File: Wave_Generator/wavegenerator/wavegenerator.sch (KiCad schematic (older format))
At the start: 61 parts, among them J1 01x05, J2 USB_B_Micro, J3 Conn_Coaxial, J4 1x2Pinheader, SW1 button, SW2 button, SW3 SP3T, U1 AZ1117E-3.3, U2 ATmega328P-AU, U3 MC33063AD, U4 MAX038CPP, Y1 16MHz

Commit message: naming changes
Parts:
- J1: footprint wavegenerator_v1:01x05_pin_header -> wavegenerator:01x05_pin_header; symbol wavegenerator_v1:PinHeaders -> wavegenerator:PinHeaders
- J2: footprint wavegenerator_v1:USB_Micro-B_Amphenol_10118194-0001LF_Horizontal -> wavegenerator:USB_Micro-B_Amphenol_10118194-0001LF_Horizontal
- J3: footprint wavegenerator_v1:BNC_connector_731000105 -> wavegenerator:BNC_connector_731000105
- J4: symbol wavegenerator_v1:1x2Pinheader -> wavegenerator:1x2Pinheader
- MOD1: footprint wavegenerator_v1:TFT_LCD_ST7735 -> wavegenerator:TFT_LCD_ST7735; symbol wavegenerator_v1:TFT_LCD -> wavegenerator:TFT_LCD
- RV1, RV2, RV3: footprint wavegenerator_v1:Potentiometer_PTV09A -> wavegenerator:Potentiometer_PTV09A
- SW3: footprint wavegenerator_v1:SP3T_OS103011MS8QP1 -> wavegenerator:SP3T_OS103011MS8QP1; symbol wavegenerator_v1:SP3T_V1 -> wavegenerator:SP3T
- U4: footprint wavegenerator_v1:MAX038CPP-W -> wavegenerator:MAX038CPP-W; symbol wavegenerator_v1:MAX038CPP -> wavegenerator:MAX038CPP
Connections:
- wire segments 121 -> 118
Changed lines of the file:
@@
 EESchema Schematic File Version 4
-LIBS:wavegenerator_v1-cache
+LIBS:wavegenerator-cache
 EELAYER 29 0
 EELAYER END
@@
 F 0 "J2" H 5857 5417 50  0000 C CNN
 F 1 "USB_B_Micro" H 5857 5326 50  0000 C CNN
-F 2 "wavegenerator_v1:USB_Micro-B_Amphenol_10118194-0001LF_Horizontal" H 5950 4900 50  0001 C CNN
+F 2 "wavegenerator:USB_Micro-B_Amphenol_10118194-0001LF_Horizontal" H 5950 4900 50  0001 C CNN
 F 3 "~" H 5950 4900 50  0001 C CNN
 	1    5800 4950
@@
 $EndComp
 $Comp
-L wavegenerator_v1:MAX038CPP U4
+L wavegenerator:MAX038CPP U4
 U 1 1 5D1E353F
 P 3350 2400
 F 0 "U4" H 3350 3970 50  0000 C CNN
 F 1 "MAX038CPP" H 3350 3879 50  0000 C CNN
-F 2 "wavegenerator_v1:MAX038CPP-W" H 3350 2400 50  0001 L BNN
+F 2 "wavegenerator:MAX038CPP-W" H 3350 2400 50  0001 L BNN
 F 3 "" H 3350 2400 50  0001 L BNN
 F 4 "MAX038CPP" H 3350 2400 50  0001 L BNN "Field4"
@@
 F 0 "RV2" H 1481 1896 50  0000 R CNN
 F 1 "20k" H 1481 1805 50  0000 R CNN
-F 2 "wavegenerator_v1:Potentiometer_PTV09A" H 1550 1850 50  0001 C CNN
+F 2 "wavegenerator:Potentiometer_PTV09A" H 1550 1850 50  0001 C CNN
 F 3 "~" H 1550 1850 50  0001 C CNN
 	1    1550 1850
@@
 F 0 "RV1" V 2200 1300 50  0000 R CNN
 F 1 "1M" V 2100 1250 50  0000 R CNN
-F 2 "wavegenerator_v1:Potentiometer_PTV09A" H 2000 1300 50  0001 C CNN
+F 2 "wavegenerator:Potentiometer_PTV09A" H 2000 1300 50  0001 C CNN
 F 3 "~" H 2000 1300 50  0001 C CNN
 	1    2000 1300
@@
 	7800 1100 8000 1100
 $Comp
-L wavegenerator_v1:SP3T_V1 SW3
+L wavegenerator:SP3T SW3
 U 1 1 5D250C2F
 P 1500 2850
 F 0 "SW3" H 1250 2350 50  0000 C CNN
 F 1 "SP3T" H 1250 2450 50  0000 C CNN
-F 2 "wavegenerator_v1:SP3T_OS103011MS8QP1" H 1500 2800 50  0001 C CNN
+F 2 "wavegenerator:SP3T_OS103011MS8QP1" H 1500 2800 50  0001 C CNN
 F 3 "" H 1500 2800 50  0001 C CNN
 	1    1500 2850
@@
 $EndComp
 $Comp
-L wavegenerator_v1:TFT_LCD MOD1
+L wavegenerator:TFT_LCD MOD1
 U 1 1 5D34C1D1
 P 8600 4400
 F 0 "MOD1" H 9728 3396 50  0000 L CNN
 F 1 "TFT_LCD" H 9728 3305 50  0000 L CNN
-F 2 "wavegenerator_v1:TFT_LCD_ST7735" H 9050 4350 50  0001 C CNN
+F 2 "wavegenerator:TFT_LCD_ST7735" H 9050 4350 50  0001 C CNN
 F 3 "" H 9050 4350 50  0001 C CNN
 	1    8600 4400
@@
 $EndComp
 $Comp
-L wavegenerator_v1:PinHeaders J1
+L wavegenerator:PinHeaders J1
 U 1 1 5D2280FD
 P 10200 800
 F 0 "J1" H 10100 850 50  0000 C CNN
 F 1 "01x05" H 10100 750 50  0000 C CNN
-F 2 "wavegenerator_v1:01x05_pin_header" H 10200 800 50  0001 C CNN
+F 2 "wavegenerator:01x05_pin_header" H 10200 800 50  0001 C CNN
 F 3 "~" H 10200 800 50  0001 C CNN
 	1    10200 800
@@
 $EndComp
 $Comp
-L wavegenerator_v1:1x2Pinheader J4
+L wavegenerator:1x2Pinheader J4
 U 1 1 5D3E4848
 P 5850 2200
@@
 F 0 "J3" H 6300 2700 50  0000 L CNN
 F 1 "Conn_Coaxial" H 6200 2600 50  0000 L CNN
-F 2 "wavegenerator_v1:BNC_connector_731000105" H 6350 2450 50  0001 C CNN
+F 2 "wavegenerator:BNC_connector_731000105" H 6350 2450 50  0001 C CNN
 F 3 " ~" H 6350 2450 50  0001 C CNN
 	1    6350 2450
@@
 	1550 1300 1750 1300
 Wire Wire Line
-	4050 3200 4050 2950
-Connection ~ 4050 2950
-Wire Wire Line
 	4050 3500 4050 3650
-Connection ~ 4050 3650
 Wire Wire Line
 	4050 3400 4200 3400
@@
 F 0 "RV3" H 4200 2000 50  0000 C CNN
 F 1 "1k" H 4200 2100 50  0000 C CNN
-F 2 "wavegenerator_v1:Potentiometer_PTV09A" H 4350 2050 50  0001 C CNN
+F 2 "wavegenerator:Potentiometer_PTV09A" H 4350 2050 50  0001 C CNN
 F 3 "~" H 4350 2050 50  0001 C CNN
 	1    4350 2050
@@
 Connection ~ 4700 1850
 Wire Wire Line
-	4050 2950 4050 2700
-Connection ~ 4050 2700
-Wire Wire Line
-	4050 2700 4050 2450
-Connection ~ 4050 3200
-Wire Wire Line
-	2650 3050 2650 3250
-Connection ~ 2650 3450
-Connection ~ 2650 3250
-Wire Wire Line
-	2650 3250 2650 3450
-Wire Wire Line
 	4350 2250 4600 2250
 Wire Wire Line
@@
 Wire Wire Line
 	4600 2050 4700 2050
+Wire Wire Line
+	4050 2450 4050 3200
+Wire Wire Line
+	2650 3050 2650 3450
 $EndSCHEMATC

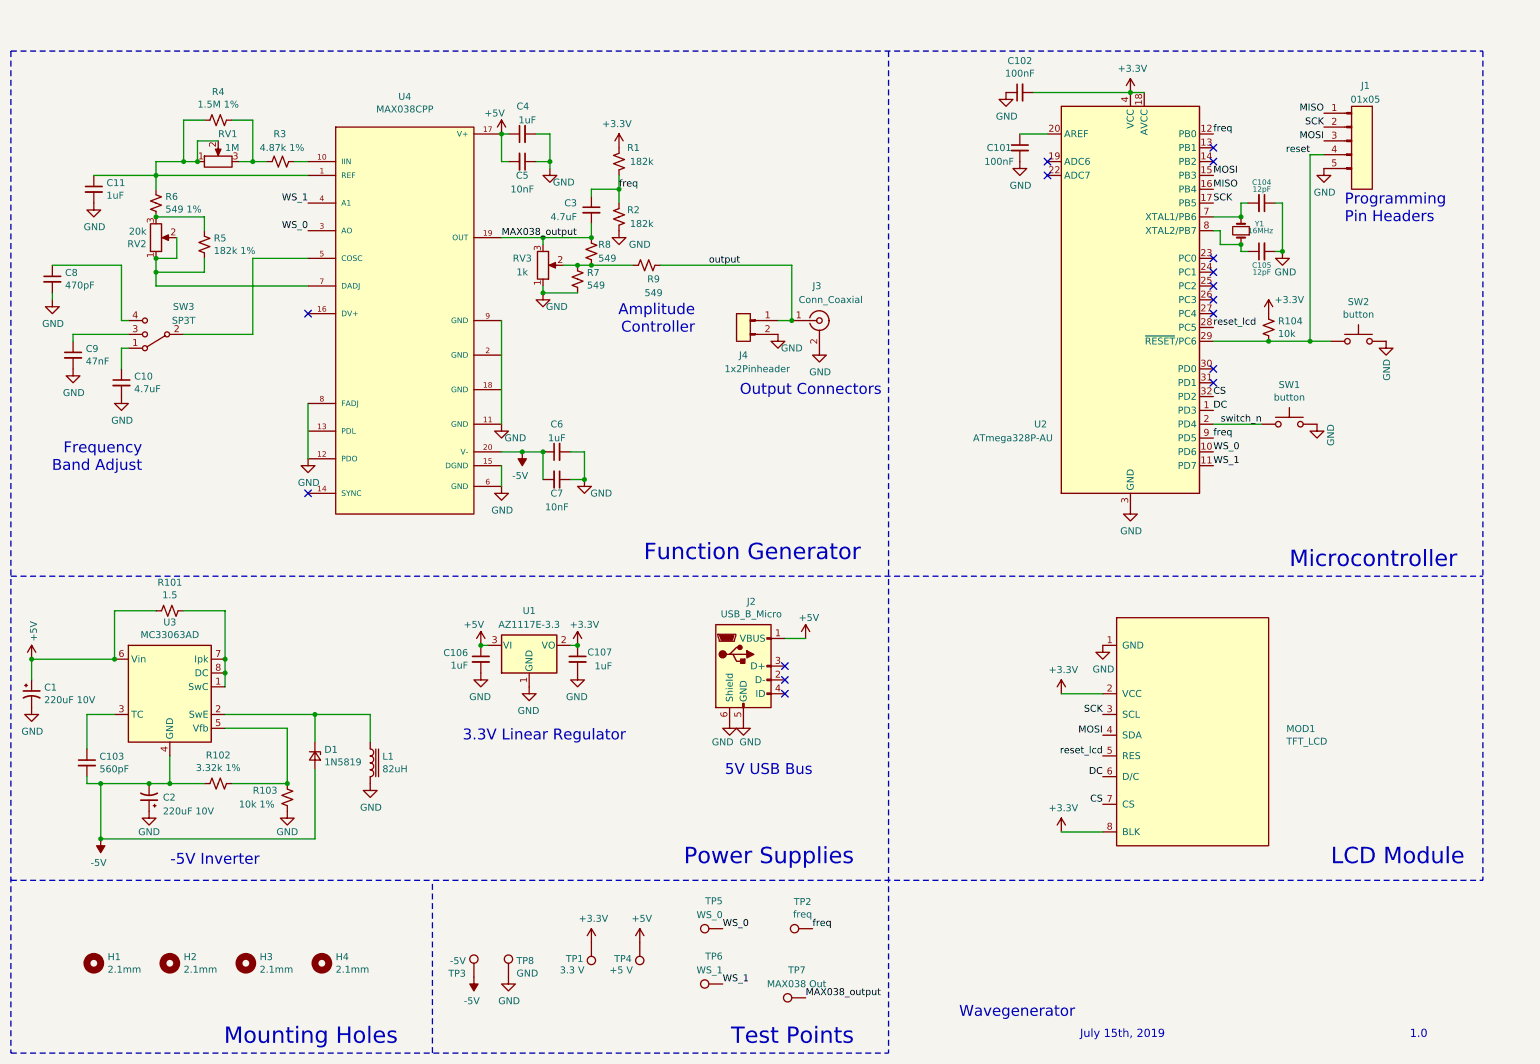
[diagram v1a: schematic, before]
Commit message: function generator schematic changes
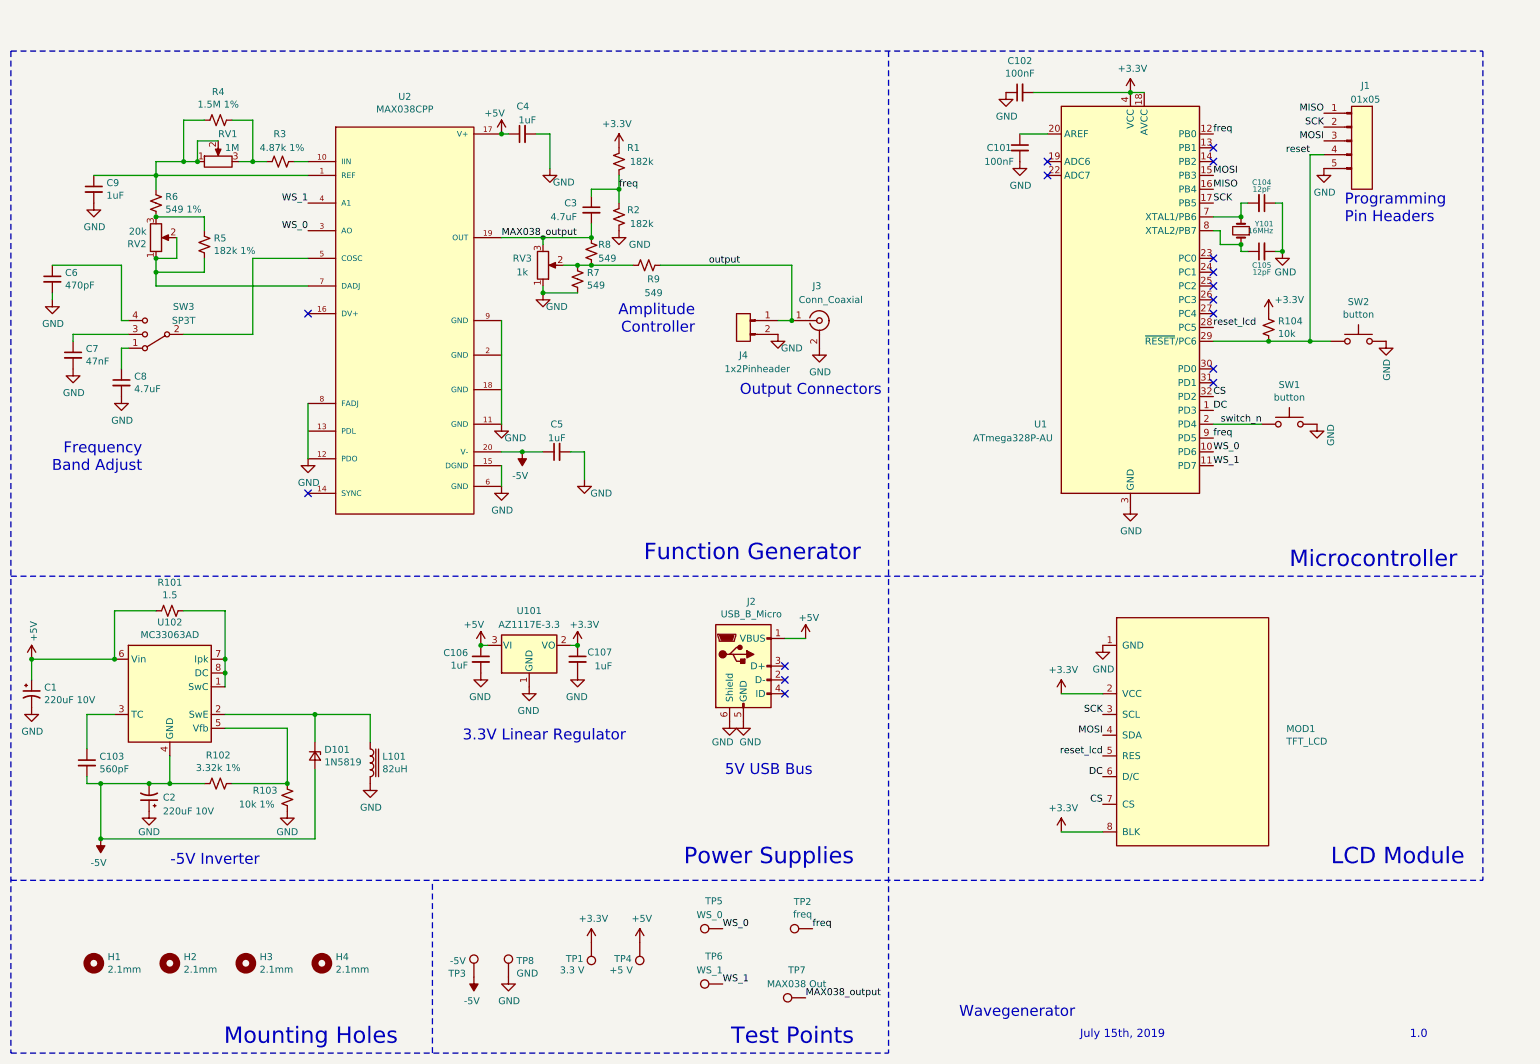
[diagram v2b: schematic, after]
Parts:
- removed C5, C7: 10nF, Capacitor_THT:C_Rect_L4.0mm_W2.5mm_P2.50mm, symbol Device:C_Small
- renumbered C6 to C5, C8 to C6, C9 to C7, C10 to C8, C11 to C9, D1 to D101, L1 to L101, U2 to U1, U1 to U101, U3 to U102, U4 to U2, Y1 to Y101
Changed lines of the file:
@@
 Connection ~ 1650 5800
 $Comp
-L Device:D_Zener_Small D1
+L Device:D_Zener_Small D101
 U 1 1 5D1C049C
 P 2700 5600
-F 0 "D1" V 2654 5668 50  0000 L CNN
+F 0 "D101" V 2654 5668 50  0000 L CNN
 F 1 "1N5819" V 2745 5668 50  0000 L CNN
 F 2 "Diode_SMD:D_SOD-123" V 2700 5600 50  0001 C CNN
@@
 $EndComp
 $Comp
-L Device:L_Core_Iron L1
+L Device:L_Core_Iron L101
 U 1 1 5D1C1934
 P 3100 5650
-F 0 "L1" H 3188 5696 50  0000 L CNN
+F 0 "L101" H 3188 5696 50  0000 L CNN
 F 1 "82uH" H 3188 5605 50  0000 L CNN
 F 2 "Inductor_SMD:L_7.3x7.3_H3.5" H 3100 5650 50  0001 C CNN
@@
 	2050 5000 2050 5100
 $Comp
-L Regulator_Switching:MC33063AD U3
+L Regulator_Switching:MC33063AD U102
 U 1 1 5D1E6E42
 P 1650 5100
-F 0 "U3" H 1650 5567 50  0000 C CNN
+F 0 "U102" H 1650 5567 50  0000 C CNN
 F 1 "MC33063AD" H 1650 5476 50  0000 C CNN
 F 2 "Package_SO:SOIC-8_3.9x4.9mm_P1.27mm" H 1700 4650 50  0001 L CNN
@@
 $EndComp
 $Comp
-L Device:C_Small C8
+L Device:C_Small C6
 U 1 1 5D379378
 P 800 2150
-F 0 "C8" H 892 2196 50  0000 L CNN
+F 0 "C6" H 892 2196 50  0000 L CNN
 F 1 "470pF" H 892 2105 50  0000 L CNN
 F 2 "Capacitor_THT:C_Rect_L4.0mm_W2.5mm_P2.50mm" H 800 2150 50  0001 C CNN
@@
 	1350 2650 1300 2650
 $Comp
-L Device:C_Small C10
+L Device:C_Small C8
 U 1 1 5D37A6B1
 P 1300 2900
-F 0 "C10" H 1392 2946 50  0000 L CNN
+F 0 "C8" H 1392 2946 50  0000 L CNN
 F 1 "4.7uF" H 1392 2855 50  0000 L CNN
 F 2 "Capacitor_THT:C_Rect_L4.0mm_W2.5mm_P2.50mm" H 1300 2900 50  0001 C CNN
@@
 $EndComp
 $Comp
-L Device:C_Small C9
+L Device:C_Small C7
 U 1 1 5D379EFA
 P 950 2700
-F 0 "C9" H 1042 2746 50  0000 L CNN
+F 0 "C7" H 1042 2746 50  0000 L CNN
 F 1 "47nF" H 1042 2655 50  0000 L CNN
 F 2 "Capacitor_THT:C_Rect_L4.0mm_W2.5mm_P2.50mm" H 950 2700 50  0001 C CNN
@@
 $EndComp
 $Comp
-L wavegenerator:MAX038CPP U4
+L wavegenerator:MAX038CPP U2
 U 1 1 5D1E353F
 P 3350 2400
-F 0 "U4" H 3350 3970 50  0000 C CNN
+F 0 "U2" H 3350 3970 50  0000 C CNN
 F 1 "MAX038CPP" H 3350 3879 50  0000 C CNN
 F 2 "wavegenerator:MAX038CPP-W" H 3350 2400 50  0001 L BNN
@@
 $EndComp
 $Comp
-L Device:C_Small C11
+L Device:C_Small C9
 U 1 1 5D2356A9
 P 1100 1500
-F 0 "C11" H 1192 1546 50  0000 L CNN
+F 0 "C9" H 1192 1546 50  0000 L CNN
 F 1 "1uF" H 1192 1455 50  0000 L CNN
 F 2 "Capacitor_THT:C_Rect_L4.0mm_W2.5mm_P2.50mm" H 1100 1500 50  0001 C CNN
@@
 $EndComp
 $Comp
-L Device:C_Small C6
+L Device:C_Small C5
 U 1 1 5D248DFE
 P 4450 3400
-F 0 "C6" V 4650 3400 50  0000 C CNN
+F 0 "C5" V 4650 3400 50  0000 C CNN
 F 1 "1uF" V 4550 3400 50  0000 C CNN
 F 2 "Capacitor_THT:C_Rect_L4.0mm_W2.5mm_P2.50mm" H 4450 3400 50  0001 C CNN
@@
 	6100 4750 6250 4750
 $Comp
-L MCU_Microchip_ATmega:ATmega328P-AU U2
+L MCU_Microchip_ATmega:ATmega328P-AU U1
 U 1 1 5D258DD6
 P 8600 2300
-F 0 "U2" H 7950 1400 50  0000 C CNN
+F 0 "U1" H 7950 1400 50  0000 C CNN
 F 1 "ATmega328P-AU" H 7750 1300 50  0000 C CNN
 F 2 "Package_QFP:TQFP-32_7x7mm_P0.8mm" H 8600 2300 50  0001 C CIN
@@
 $EndComp
 $Comp
-L Device:Crystal_Small Y1
+L Device:Crystal_Small Y101
 U 1 1 5D264732
 P 9400 1800
-F 0 "Y1" V 9450 1700 39  0000 R CNN
+F 0 "Y101" V 9450 1700 39  0000 R CNN
 F 1 "16MHz" V 9400 1750 39  0000 R CNN
 F 2 "Crystal:Crystal_SMD_ECS_CSM3X-2Pin_7.6x4.1mm" H 9400 1800 50  0001 C CNN
@@
 $EndComp
 $Comp
-L Regulator_Linear:AP1117-33 U1
+L Regulator_Linear:AP1117-33 U101
 U 1 1 5D2563E2
 P 4250 4800
-F 0 "U1" H 4250 5050 50  0000 C CNN
+F 0 "U101" H 4250 5050 50  0000 C CNN
 F 1 "AZ1117E-3.3" H 4250 4950 50  0000 C CNN
 F 2 "Package_TO_SOT_SMD:SOT-223-3_TabPin2" H 4250 4600 50  0001 C CIN
@@
 $EndComp
 Connection ~ 4350 1850
-$Comp
-L Device:C_Small C5
-U 1 1 5D571033
-P 4200 1300
-F 0 "C5" V 4300 1300 50  0000 C CNN
-F 1 "10nF" V 4400 1300 50  0000 C CNN
-F 2 "Capacitor_THT:C_Rect_L4.0mm_W2.5mm_P2.50mm" H 4200 1300 50  0001 C CNN
-F 3 "~" H 4200 1300 50  0001 C CNN
-	1    4200 1300
-	0    1    1    0
-$EndComp
-Wire Wire Line
-	4050 1100 4050 1300
-Wire Wire Line
-	4050 1300 4100 1300
-Wire Wire Line
-	4300 1300 4400 1300
-Wire Wire Line
-	4400 1300 4400 1100
 Wire Wire Line
 	4400 1100 4300 1100
-Connection ~ 4400 1300
-Wire Wire Line
-	4400 1300 4400 1350
-$Comp
-L Device:C_Small C7
-U 1 1 5D5888D6
-P 4450 3600
-F 0 "C7" V 4550 3600 50  0000 C CNN
-F 1 "10nF" V 4650 3600 50  0000 C CNN
-F 2 "Capacitor_THT:C_Rect_L4.0mm_W2.5mm_P2.50mm" H 4450 3600 50  0001 C CNN
-F 3 "~" H 4450 3600 50  0001 C CNN
-	1    4450 3600
-	0    1    1    0
-$EndComp
 Wire Wire Line
 	4200 3400 4350 3400
 Wire Wire Line
-	4350 3400 4350 3600
-Connection ~ 4350 3400
-Wire Wire Line
-	4550 3600 4650 3600
-Wire Wire Line
 	4550 3400 4650 3400
 Wire Wire Line
 	4650 3400 4650 3600
-Connection ~ 4650 3600
 Wire Wire Line
 	4350 1850 4700 1850
@@
 Wire Wire Line
 	2650 3050 2650 3450
+Wire Wire Line
+	4400 1100 4400 1350
 $EndSCHEMATC
